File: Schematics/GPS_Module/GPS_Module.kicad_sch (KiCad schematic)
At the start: 70 parts, among them J1 470804001, J1 USB_B_Micro, J2 SWD_01x04_Pin, J4 Stack Male Edge Connector, Q1 AO3400A, SW1 SW_STM_RESET, SW2 SW_STM_BOOT_MODE, U1 STM32F103CBTx, U2 W25Q128JVS, U3 AMS1117-3.3, U4 LM66100DCKR, U5 LM66100DCKR, U6 LM66100DCKR, U8 ACS70331EOLC, U9 ISO1042BQDWVR, Y1 X322516MMB4SI

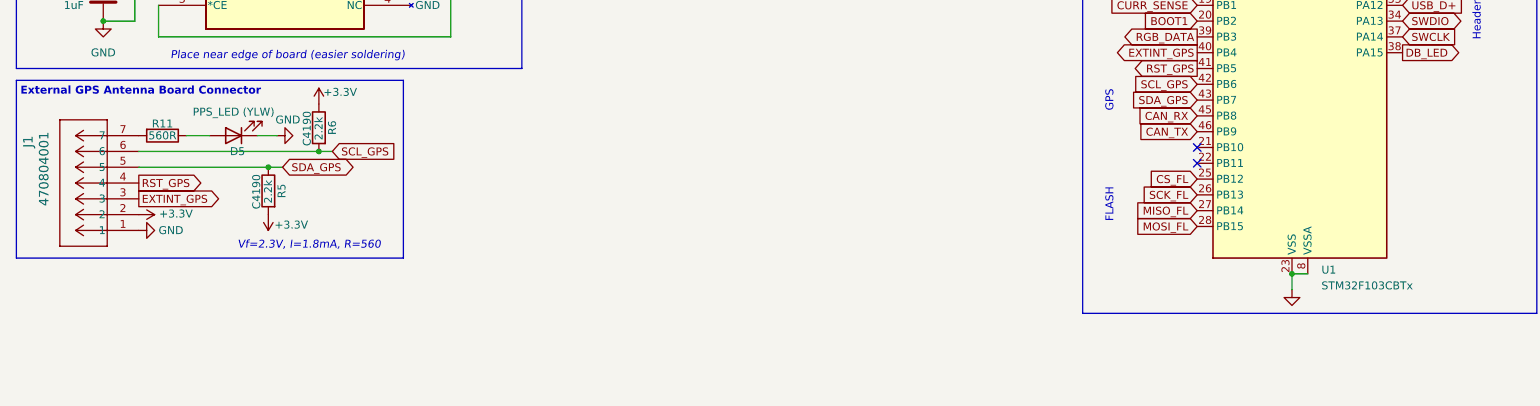
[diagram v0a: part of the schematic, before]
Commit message: Added digikey & LCSC part numbers to symbols
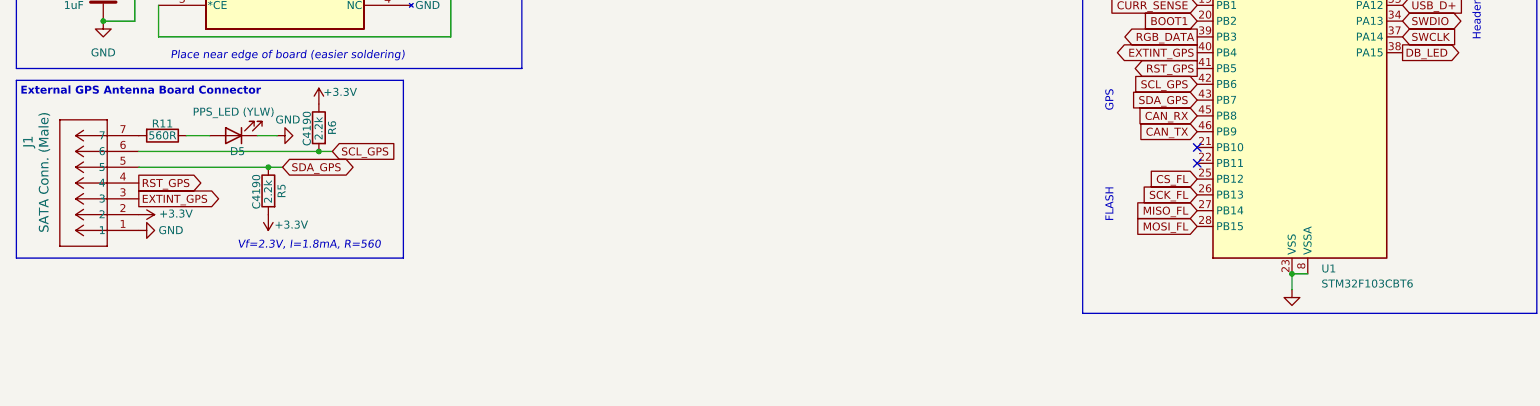
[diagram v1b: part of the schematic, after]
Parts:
- BZ1: Digikey (none) -> 490-4698-1-ND
- D4, D6: Digikey (none) -> 1568-COM-16347CT-ND
- J1: value 470804001 -> SATA Conn. (Male)
- J2: Digikey (none) -> 2057-PH1RB-04-UA-ND
- U1: value STM32F103CBTx -> STM32F103CBT6; LCSC (none) -> C8304
- U8: Digikey ACS70331EOLCTR-2P5U3 -> 620-ACS70331EOLCTR-2P5U3CT-ND
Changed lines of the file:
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@@
   (title_block
     (title "QRET 23-24 SRAD GPS Module")
-    (date "2024-03-13")
+    (date "2024-03-18")
     (rev "V1.0")
     (company "Queen's Rocket Engineering Team")
@@
       (effects (font (size 1.27 1.27)) hide)
     )
+    (property "Digikey" "2057-PH1RB-04-UA-ND" (at 388.62 170.18 0)
+      (effects (font (size 1.27 1.27)) hide)
+    )
     (pin "1")
     (pin "2")
@@
       (effects (font (size 1.27 1.27)) hide)
     )
-    (property "Digikey" "ACS70331EOLCTR-2P5U3" (at 43.18 40.64 0)
+    (property "Digikey" "620-ACS70331EOLCTR-2P5U3CT-ND" (at 43.18 40.64 0)
       (effects (font (size 1.27 1.27)) hide)
     )
@@
       (effects (font (size 1.27 1.27)) (justify left top) hide)
     )
+    (property "Digikey" "1568-COM-16347CT-ND" (at 404.495 80.645 0)
+      (effects (font (size 1.27 1.27)) hide)
+    )
     (pin "1")
     (pin "2")
@@
   (symbol (lib_id "MCU_ST_STM32F1:STM32F103CBTx") (at 219.71 130.81 0) (unit 1)
     (in_bom yes) (on_board yes) (dnp no) (fields_autoplaced)
-    (property "Reference" "U1" (at 224.4441 168.275 0)
+    (property "Reference" "U1" (at 224.4441 168.0901 0)
       (effects (font (size 1.27 1.27)) (justify left))
     )
-    (property "Value" "STM32F103CBTx" (at 224.4441 170.815 0)
+    (property "Value" "STM32F103CBT6" (at 224.4441 170.5143 0)
       (effects (font (size 1.27 1.27)) (justify left))
     )
@@
       (effects (font (size 1.27 1.27)) hide)
     )
+    (property "LCSC" "C8304" (at 219.71 130.81 0)
+      (effects (font (size 1.27 1.27)) hide)
+    )
     (pin "1")
     (pin "10")
@@
       (effects (font (size 1.27 1.27)) hide)
     )
+    (property "Digikey" "490-4698-1-ND" (at 399.415 28.575 0)
+      (effects (font (size 1.27 1.27)) hide)
+    )
     (pin "1")
     (pin "2")
@@
       (effects (font (size 1.27 1.27)) (justify left top) hide)
     )
+    (property "Digikey" "1568-COM-16347CT-ND" (at 384.175 80.645 0)
+      (effects (font (size 1.27 1.27)) hide)
+    )
     (pin "1")
     (pin "2")
@@
       (effects (font (size 1.524 1.524)) (justify left))
     )
-    (property "Value" "470804001" (at 19.05 146.05 90)
+    (property "Value" "SATA Conn. (Male)" (at 19.05 142.875 90)
       (effects (font (size 1.524 1.524)) (justify left))
     )

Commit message: checking lcsc and digikey numbers
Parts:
- U4, U5, U6: Digikey 296-53541-1-ND -> (none); LCSC (none) -> C2869734
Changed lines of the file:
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@@
       (effects (font (size 1.27 1.27) italic) hide)
     )
-    (property "Digikey" "296-53541-1-ND" (at 57.785 123.19 0)
+    (property "LCSC" "C2869734" (at 57.785 123.19 0)
       (effects (font (size 1.27 1.27)) hide)
     )
@@
       (effects (font (size 1.27 1.27) italic) hide)
     )
-    (property "Digikey" "296-53541-1-ND" (at 57.785 85.09 0)
+    (property "LCSC" "C2869734" (at 57.785 85.09 0)
       (effects (font (size 1.27 1.27)) hide)
     )
@@
       (effects (font (size 1.27 1.27) italic) hide)
     )
-    (property "Digikey" "296-53541-1-ND" (at 57.785 104.14 0)
+    (property "LCSC" "C2869734" (at 57.785 104.14 0)
       (effects (font (size 1.27 1.27)) hide)
     )

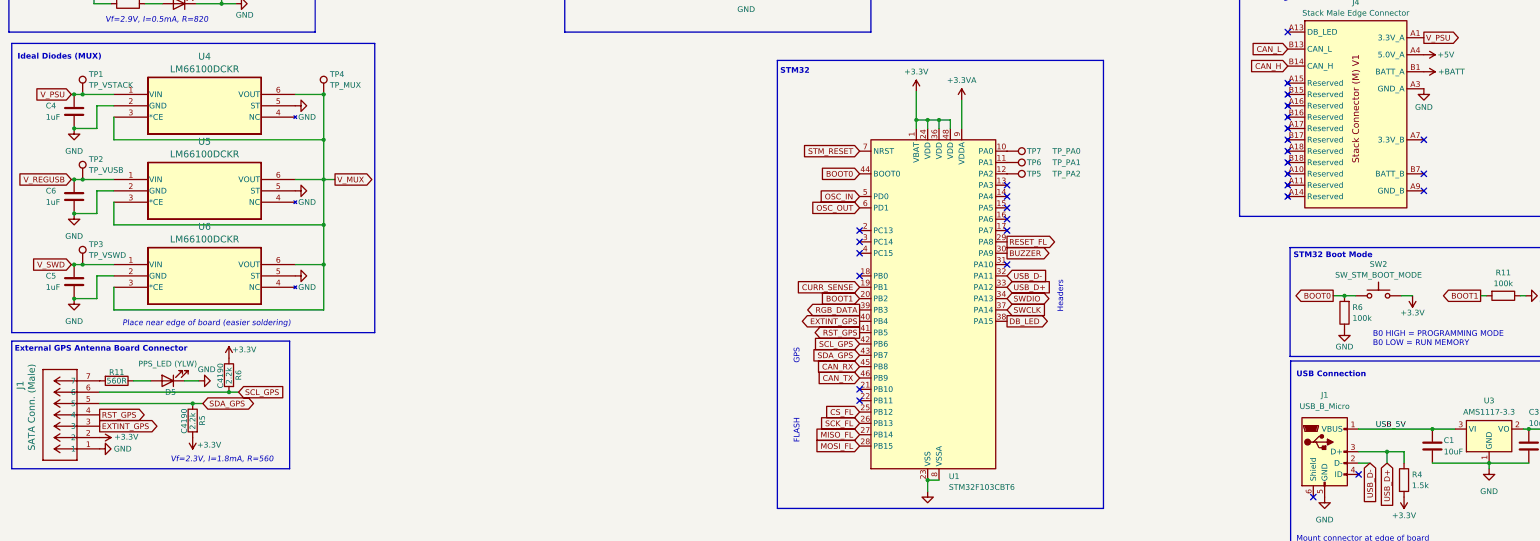
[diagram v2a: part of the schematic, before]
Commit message: Verified part numbers & made ERC pass
Also cleaned up unnecessary footprints & added bulk filtering capacitor to GPS antenna board
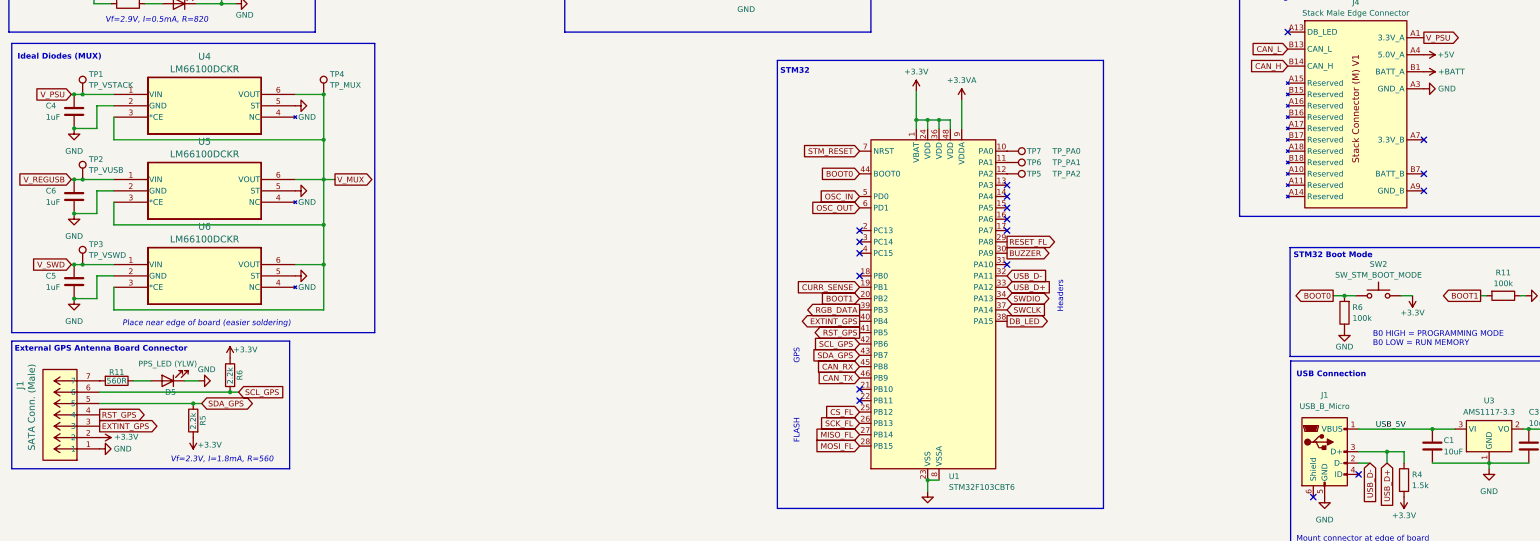
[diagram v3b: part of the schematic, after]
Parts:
- J1: footprint footprints:CONN_47080-4001_MOL_SATA -> CONN_47080-4001_MOL
- J4, TP1, TP10, TP2, TP3, TP4, TP5, TP6, TP7, TP8, TP9: now left out of the parts list
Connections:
- no-connect marks 30 -> 19

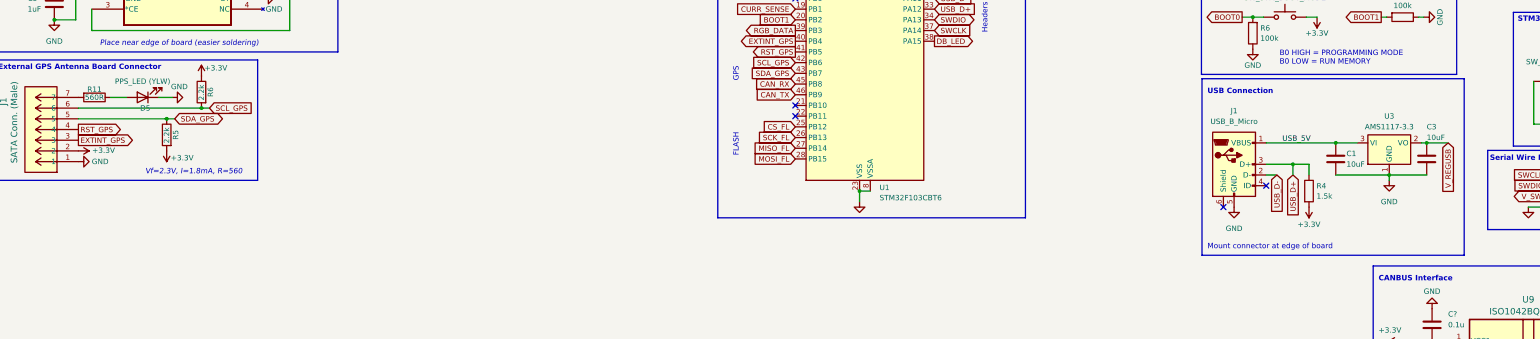
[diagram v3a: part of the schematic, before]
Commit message: PCB Adjustments + Add USB-C port (DRC pass)
- Rerouted several traces to reduce via hopping
- Routed CANBUS wires as differential pair
- Rearranged some items
- Swapped USB-MicroB port for USB-C port
- Added silkscreen labels
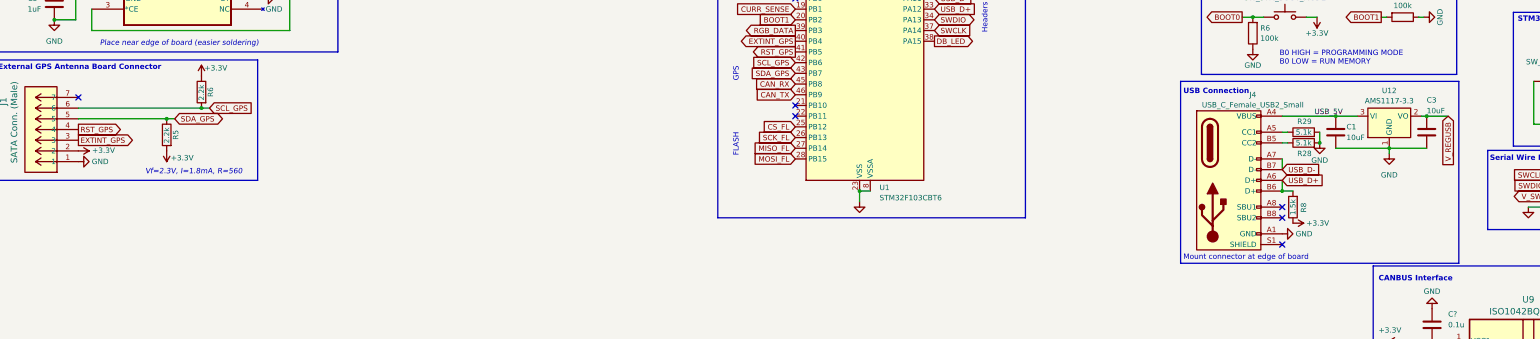
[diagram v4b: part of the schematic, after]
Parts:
- removed D5: PPS_LED (YLW), LED_SMD:LED_0603_1608Metric, symbol Device:LED
- removed J1: USB_B_Micro, Connector_USB:USB_Micro-B_Amphenol_10118194_Horizontal, symbol Connector:USB_B_Micro
- removed R11: 560R, Resistor_SMD:R_0603_1608Metric, symbol Device:R
- removed R4: 1.5k, Resistor_SMD:R_0603_1608Metric, symbol Device:R
- removed U3: AMS1117-3.3, Package_TO_SOT_SMD:SOT-223-3_TabPin2, symbol Regulator_Linear:AMS1117-3.3
- added J4: USB_C_Female_USB2_Small, footprints:USB_C_DB-108PWB, symbol USB_C:USB_C_Female_USB2_Small
- added R28, R29: 5.1k, Resistor_SMD:R_0603_1608Metric, symbol Device:R
- added R8: 1.5k, Resistor_SMD:R_0603_1608Metric, symbol Device:R
- added U12: AMS1117-3.3, Package_TO_SOT_SMD:SOT-223-3_TabPin2, symbol Regulator_Linear:AMS1117-3.3
- J1: footprint CONN_47080-4001_MOL -> footprints:CONN_47080-4001_MOL_SATA
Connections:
- net +3.3V: now also R8.1
- net GND: now also J4.A1 (GND), J4.A12 (GND), J4.B1 (GND), J4.B12 (GND), R28.2, R29.2, U12.1 (GND)
- net USB_5V: now also J4.A4 (VBUS), J4.A9 (VBUS), J4.B4 (VBUS), J4.B9 (VBUS), U12.3 (VI)
- net USB_D+: now also J4.A6 (D+), J4.B6 (D+), R8.2
- net USB_D-: now also J4.A7 (D-), J4.B7 (D-)
- net V_REGUSB: now also U12.2 (VO)
- new net: J4.A5 (CC1), R29.1
- new net: J4.B5 (CC2), R28.1
- no-connect marks 19 -> 21
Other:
- moved on the sheet: C1, C3
